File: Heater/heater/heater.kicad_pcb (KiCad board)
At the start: 2 copper layers, 63.5 x 40.1 mm, 10 parts, among them J1 , Q1 IRF7401TRPBF

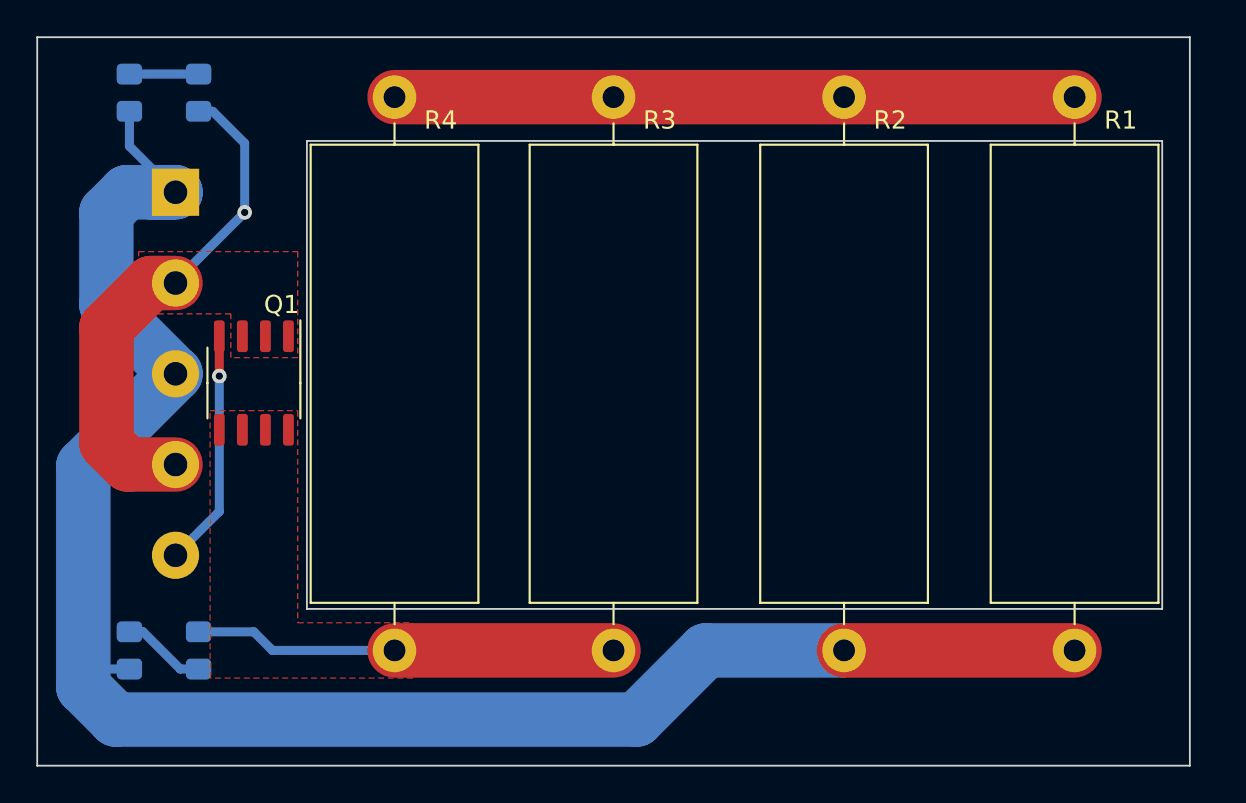
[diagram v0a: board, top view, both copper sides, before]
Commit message: update heater pcb
Heater pcb now includes 12V for fan, and a FET to switch the fans on and off
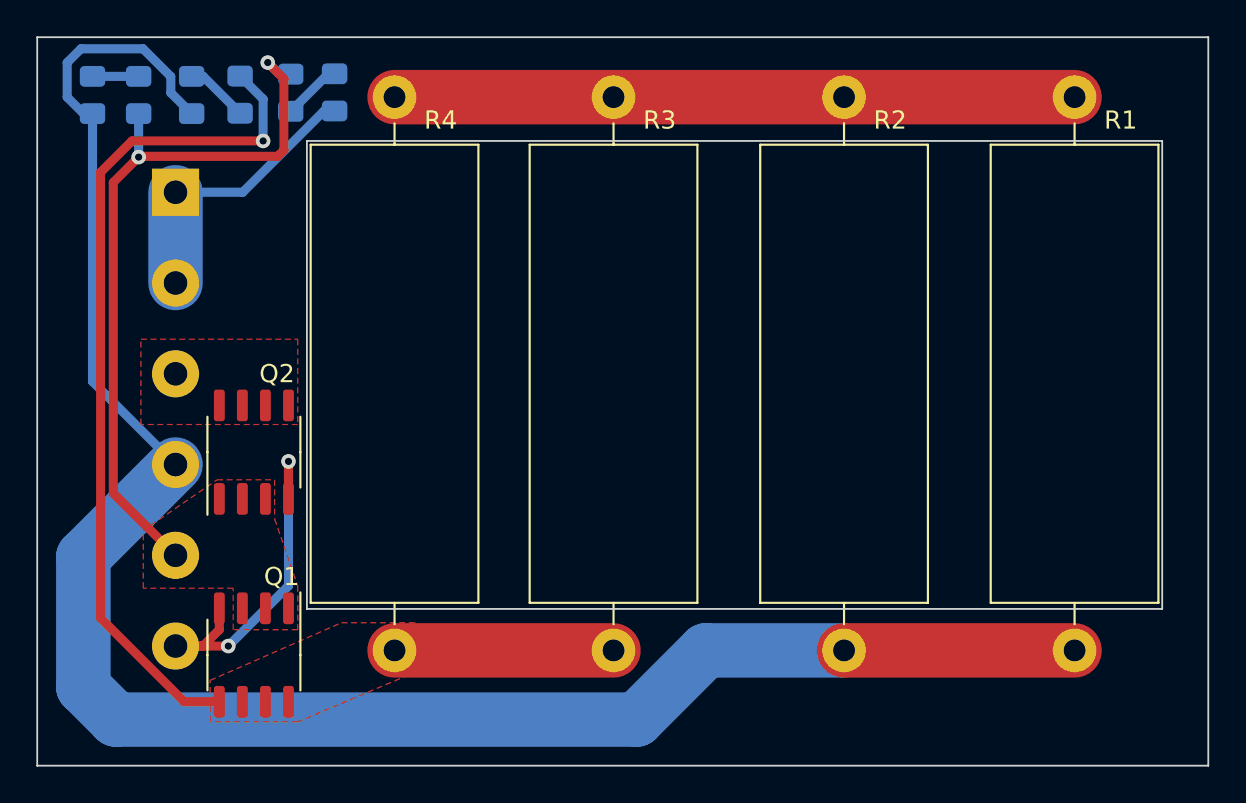
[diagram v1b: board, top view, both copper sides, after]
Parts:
- added D3: AMBER, LED_SMD:LED_0805_2012Metric_Pad1.15x1.40mm_HandSolder, B.Cu at (34.3, 21.3)
- added Q2: IRF7401TRPBF, Package_SO:SO-8_3.9x4.9mm_P1.27mm, F.Cu at (32.3, 41.1)
- added R7: 1k, Resistor_SMD:R_0805_2012Metric_Pad1.15x1.40mm_HandSolder, B.Cu at (36.7, 21.3)
- J1: footprint TerminalBlock_Phoenix:TerminalBlock_Phoenix_MKDS-1,5-5_1x05_P5.00mm_Horizontal -> TerminalBlock_Phoenix:TerminalBlock_Phoenix_MKDS-1,5-6_1x06_P5.00mm_Horizontal
- moved R5 30.8 mm to (28.8, 21.5)
- moved D1 30.7 mm to (31.5, 21.5)
- moved Q1 15.0 mm to (32.3, 52.3)
- moved D2 3.30 mm to (25.9, 21.5)
- moved R6 2.04 mm to (23.4, 21.5)
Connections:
- J1 pad 1: VCC -> +12V
- J1 pad 2: GND -> +12V
- J1 pad 3: VCC -> /Fan_Lowside
- J1 pad 4: GND -> VCC
- J1 pad 5: /Heat_Control -> GND
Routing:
- net Net-(D1-Pad1): track 22.6 -> 58.8 mm, vias 0 -> 1
- net +12V: track 0.00 -> 15.6 mm
- net GND: track 28.0 -> 41.2 mm, vias 1 -> 2
- net /Heat_Control: track 13.1 -> 20.5 mm, vias 1 -> 2
- net VCC: track 100.9 -> 105.4 mm
- net Net-(D3-Pad2): track 0.00 -> 3.27 mm
- net Net-(D2-Pad2): track 3.81 -> 2.54 mm
- net Net-(D1-Pad2): track 4.66 -> 3.51 mm
- added copper zone on F.Cu, net /Fan_Lowside
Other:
- board size 63.5 x 40.1 mm -> 64.5 x 40.1 mm
- board text added: "6"
- board text added: "Connector: 1: 12V | 2: Fan+ | 3: Fan- | 4: Power | 5: GND | 6: Data"
- board text added: "D1: Heater On"
- board text added: "D2: Power"
- board text added: "D3: 12V"
- board text removed: "5"
- board text removed: "Connector: 1: Power | 2: GND | 3: Fan+ | 4: Fan- | 5: Data"
